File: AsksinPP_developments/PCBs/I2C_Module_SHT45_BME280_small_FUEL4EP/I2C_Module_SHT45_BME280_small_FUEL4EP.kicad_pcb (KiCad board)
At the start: 2 copper layers, 22 x 17 mm, 13 parts, among them J1 Conn_01x04, U1 BME280, U2 SHT45-AD1B-R2

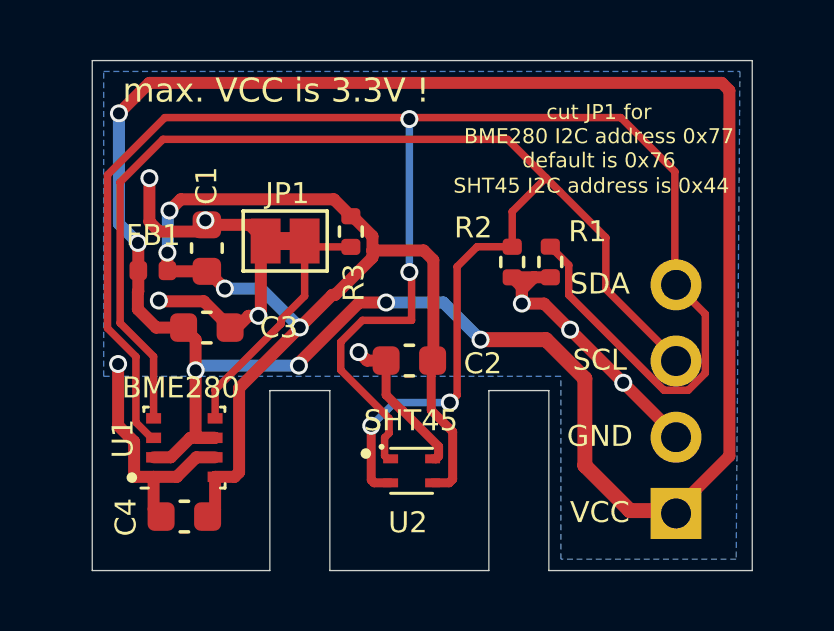
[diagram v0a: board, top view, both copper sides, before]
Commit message: PCBs: HB_Stamp_ATMega1284P_FUEL4EP and I2C_Module_SHT45_BME280_small_FUEL4EP: make I2C sockets fitting each other
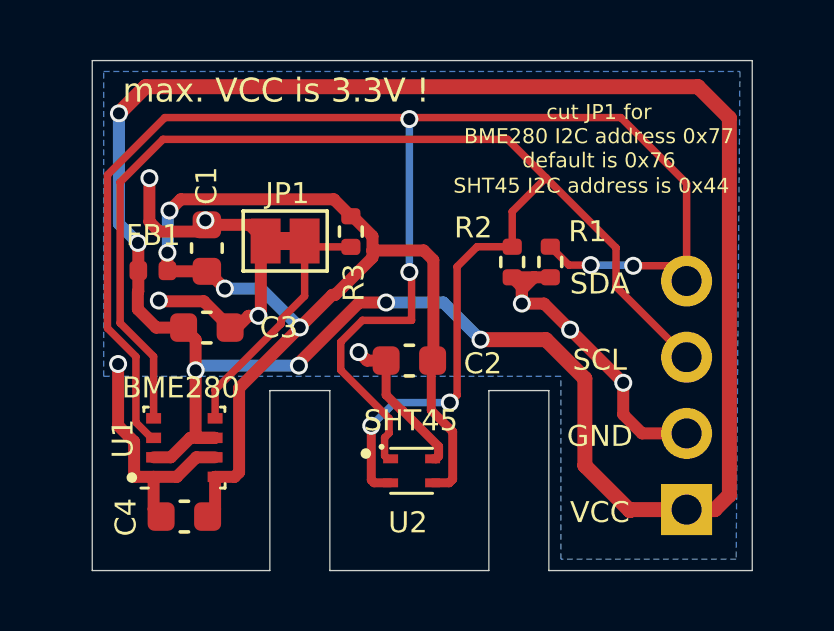
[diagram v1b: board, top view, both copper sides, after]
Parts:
- moved J1 0.37 mm to (19.8, -2.03)
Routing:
- net /SDA: track 59.0 -> 52.0 mm, vias 2 -> 4
- net GND: track 35.6 -> 36.3 mm
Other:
- board text added: "SHT45 BME280 I2C Modul small (C) FUEL4EP V1.1 01/2024"
- board text removed: "SHT45 BME280 I2C Modul small (C) FUEL4EP V1.0 01/2024"

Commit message: PCBs: fix of I2C Pull-up resistors that were wrongly tied to GND
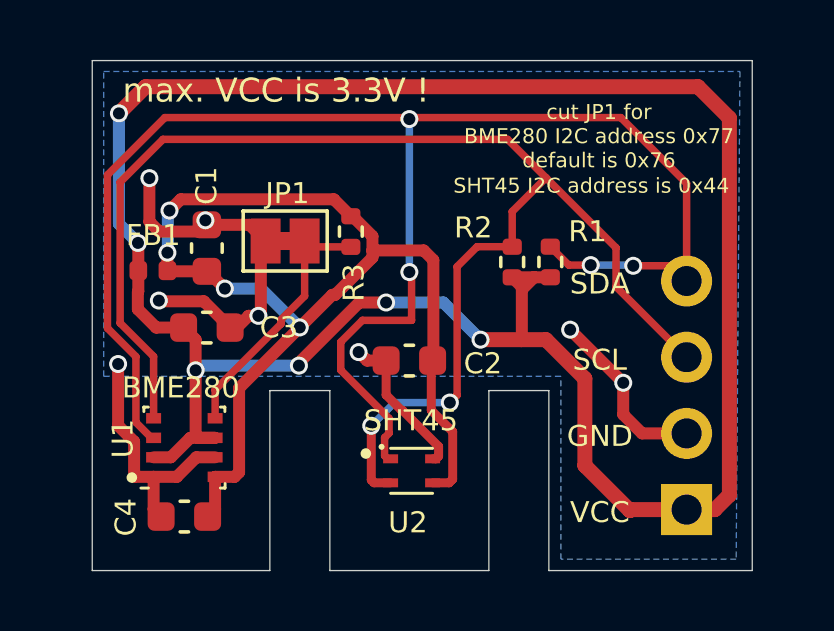
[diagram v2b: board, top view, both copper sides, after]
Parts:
- R1, R2: value 4.7k -> 10k
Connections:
- R1 pad 2: GND -> VCC
- R2 pad 2: GND -> VCC
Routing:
- net GND: track 36.3 -> 31.0 mm, vias 9 -> 8
- net VCC: track 72.6 -> 76.6 mm
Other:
- board text added: "SHT45 BME280 I2C Modul small (C) FUEL4EP V1.2 02/2024"
- board text removed: "SHT45 BME280 I2C Modul small (C) FUEL4EP V1.1 01/2024"
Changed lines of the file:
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@@
   (title_block
     (title "I2C_Module_SHT45_BME280_FUEL4EP")
-    (date "2023-12-15")
-    (rev "V1.1")
+    (date "2024-02-08")
+    (rev "V1.2")
     (company "(c) FUEL4EP")
   )
@@
     (descr "Resistor SMD 0402 (1005 Metric), square (rectangular) end terminal, IPC_7351 nominal, (Body size source: IPC-SM-782 page 72, https://www.pcb-3d.com/wordpress/wp-content/uploads/ipc-sm-782a_amendment_1_and_2.pdf), generated with kicad-footprint-generator")
     (tags "resistor")
-    (property "LCSC" "C25900")
+    (property "LCSC" "C25744")
     (property "Sheetfile" "I2C_Module_SHT45_BME280_small_FUEL4EP.kicad_sch")
     (property "Sheetname" "")
@@
       (effects (font (size 0.7 0.7) (thickness 0.15)))
     )
-    (fp_text value "4.7k" (at -0.12 -0.015 -270) (layer "F.Fab")
+    (fp_text value "10k" (at -0.12 -0.015 -270) (layer "F.Fab")
       (effects (font (size 0.7 0.7) (thickness 0.15)))
     )
@@
       (net 4 "/SDA") (pintype "passive"))
     (pad "2" smd roundrect (at 0.51 0 270) (size 0.54 0.64) (layers "F.Cu" "F.Paste" "F.Mask") (roundrect_rratio 0.25)
-      (net 2 "GND") (pintype "passive"))
+      (net 1 "VCC") (pintype "passive"))
     (model "${KICAD6_3DMODEL_DIR}/Resistor_SMD.3dshapes/R_0402_1005Metric.wrl"
       (offset (xyz 0 0 0))
@@
     (descr "Resistor SMD 0402 (1005 Metric), square (rectangular) end terminal, IPC_7351 nominal, (Body size source: IPC-SM-782 page 72, https://www.pcb-3d.com/wordpress/wp-content/uploads/ipc-sm-782a_amendment_1_and_2.pdf), generated with kicad-footprint-generator")
     (tags "resistor")
-    (property "LCSC" "C25900")
+    (property "LCSC" "C25744")
     (property "Sheetfile" "I2C_Module_SHT45_BME280_small_FUEL4EP.kicad_sch")
     (property "Sheetname" "")
@@
       (effects (font (size 0.7 0.7) (thickness 0.15)))
     )
-    (fp_text value "4.7k" (at -0.2 -0.1 -270) (layer "F.Fab")
+    (fp_text value "10k" (at -0.2 -0.1 -270) (layer "F.Fab")
       (effects (font (size 0.7 0.7) (thickness 0.15)))
     )
@@
       (net 3 "/SCL") (pintype "passive"))
     (pad "2" smd roundrect (at 0.51 0 270) (size 0.54 0.64) (layers "F.Cu" "F.Paste" "F.Mask") (roundrect_rratio 0.25)
-      (net 2 "GND") (pintype "passive"))
+      (net 1 "VCC") (pintype "passive"))
     (model "${KICAD6_3DMODEL_DIR}/Resistor_SMD.3dshapes/R_0402_1005Metric.wrl"
       (offset (xyz 0 0 0))
@@
   (gr_line (start 13.22 0) (end 7.92 0) (layer "Edge.Cuts") (width 0.0381))
   (gr_line (start 22 -17) (end 22 0) (layer "Edge.Cuts") (width 0.0381))
-  (gr_text "SHT45 BME280\nI2C Modul small\n(C) FUEL4EP\nV1.1\n01/2024" (at 10.795 -9.144) (layer "B.SilkS")
+  (gr_text "SHT45 BME280\nI2C Modul small\n(C) FUEL4EP\nV1.2\n02/2024" (at 10.795 -9.144) (layer "B.SilkS")
     (effects (font (size 0.7 0.7) (thickness 0.1524)) (justify mirror))
   )
@@
     (effects (font (size 0.8 0.8) (thickness 0.1524)))
   )
+  (segment (start 14.32 -7.716) (end 14.300884 -7.696884) (width 0.4) (layer "F.Cu") (net 1))
   (segment (start 17.92 -2) (end 16.42 -3.5) (width 0.5) (layer "F.Cu") (net 1))
   (segment (start 3.27 -4.425) (end 2.62 -3.775) (width 0.4) (layer "F.Cu") (net 1))
   (segment (start 8.900493 -8.935823) (end 9.794735 -8.935823) (width 0.4) (layer "F.Cu") (net 1))
   (segment (start 20.752 -2.032) (end 21.238 -2.518) (width 0.5) (layer "F.Cu") (net 1))
+  (segment (start 15.269 -9.777) (end 14.73 -9.777) (width 0.4) (layer "F.Cu") (net 1))
   (segment (start 21.238 -15.084) (end 20.193 -16.129) (width 0.5) (layer "F.Cu") (net 1))
   (segment (start 2.62 -3.775) (end 2.045 -3.775) (width 0.4) (layer "F.Cu") (net 1))
@@
   (segment (start 21.238 -2.518) (end 21.238 -15.084) (width 0.5) (layer "F.Cu") (net 1))
   (segment (start 17.92 -2) (end 17.952 -2.032) (width 0.5) (layer "F.Cu") (net 1))
+  (segment (start 14.32 -9.367) (end 14.73 -9.777) (width 0.4) (layer "F.Cu") (net 1))
+  (segment (start 14.73 -9.777) (end 14.001 -9.777) (width 0.4) (layer "F.Cu") (net 1))
   (segment (start 20.193 -16.129) (end 1.778 -16.129) (width 0.5) (layer "F.Cu") (net 1))
   (segment (start 17.952 -2.032) (end 19.812 -2.032) (width 0.5) (layer "F.Cu") (net 1))
-  (segment (start 15.123116 -7.696884) (end 12.9425 -7.696884) (width 0.5) (layer "F.Cu") (net 1))
   (segment (start 1.5205 -8.710257) (end 2.130757 -8.1) (width 0.4) (layer "F.Cu") (net 1))
   (segment (start 1.5205 -9.289743) (end 1.5205 -8.710257) (width 0.4) (layer "F.Cu") (net 1))
@@
   (segment (start 2.130757 -8.1) (end 3.045 -8.1) (width 0.4) (layer "F.Cu") (net 1))
   (segment (start 16.42 -6.4) (end 15.123116 -7.696884) (width 0.5) (layer "F.Cu") (net 1))
+  (segment (start 14.32 -9.454) (end 13.999 -9.775) (width 0.4) (layer "F.Cu") (net 1))
   (segment (start 1.535 -9.304243) (end 1.5205 -9.289743) (width 0.4) (layer "F.Cu") (net 1))
   (segment (start 3.52 -4.425) (end 3.445 -4.5) (width 0.4) (layer "F.Cu") (net 1))
   (segment (start 16.42 -3.5) (end 16.42 -6.4) (width 0.5) (layer "F.Cu") (net 1))
   (segment (start 1.535 -10) (end 1.535 -10.911) (width 0.4) (layer "F.Cu") (net 1))
+  (segment (start 14.32 -9.367) (end 14.32 -7.716) (width 0.4) (layer "F.Cu") (net 1))
   (segment (start 4.095 -4.425) (end 3.27 -4.425) (width 0.4) (layer "F.Cu") (net 1))
   (segment (start 3.445 -7.7) (end 3.045 -8.1) (width 0.4) (layer "F.Cu") (net 1))
   (segment (start 6.888742 -6.831258) (end 6.888742 -6.924072) (width 0.4) (layer "F.Cu") (net 1))
   (segment (start 4.095 -4.425) (end 3.52 -4.425) (width 0.4) (layer "F.Cu") (net 1))
+  (segment (start 14.300884 -7.696884) (end 12.9425 -7.696884) (width 0.5) (layer "F.Cu") (net 1))
   (segment (start 19.812 -2.032) (end 20.752 -2.032) (width 0.5) (layer "F.Cu") (net 1))
+  (segment (start 15.123116 -7.696884) (end 14.300884 -7.696884) (width 0.5) (layer "F.Cu") (net 1))
   (via (at 9.794735 -8.935823) (size 0.6) (drill 0.4) (layers "F.Cu" "B.Cu") (net 1))
   (via (at 1.524 -10.922) (size 0.6) (drill 0.4) (layers "F.Cu" "B.Cu") (net 1))
@@
   (segment (start 18.328 -4.572) (end 19.812 -4.572) (width 0.4) (layer "F.Cu") (net 2))
   (segment (start 11.457132 -3.725) (end 11.345 -3.725) (width 0.3) (layer "F.Cu") (net 2))
-  (segment (start 14.32 -8.9) (end 14.32 -9.454) (width 0.4) (layer "F.Cu") (net 2))
   (segment (start 5.62 -8.572728) (end 5.539014 -8.491742) (width 0.4) (layer "F.Cu") (net 2))
   (segment (start 10.316 -5.334) (end 9.795 -5.855) (width 0.3) (layer "F.Cu") (net 2))
@@
   (segment (start 10.348132 -5.334) (end 11.545 -4.137132) (width 0.3) (layer "F.Cu") (net 2))
   (segment (start 5.62 -10.825) (end 5.62 -8.572728) (width 0.4) (layer "F.Cu") (net 2))
-  (segment (start 15.269 -9.777) (end 14.73 -9.777) (width 0.4) (layer "F.Cu") (net 2))
   (segment (start 1.905 -11.625757) (end 1.905 -13.081) (width 0.4) (layer "F.Cu") (net 2))
   (segment (start 17.7 -6.26) (end 17.7 -5.2) (width 0.4) (layer "F.Cu") (net 2))
   (segment (start 5.211742 -8.491742) (end 5.539014 -8.491742) (width 0.4) (layer "F.Cu") (net 2))
-  (segment (start 15.93 -8.03) (end 15.06 -8.9) (width 0.4) (layer "F.Cu") (net 2))
-  (segment (start 14.32 -8.9) (end 14.32 -9.367) (width 0.4) (layer "F.Cu") (net 2))
-  (segment (start 14.32 -9.367) (end 14.73 -9.777) (width 0.4) (layer "F.Cu") (net 2))
-  (segment (start 14.73 -9.777) (end 14.001 -9.777) (width 0.4) (layer "F.Cu") (net 2))
   (segment (start 9.795 -5.855) (end 9.795 -7) (width 0.3) (layer "F.Cu") (net 2))
   (segment (start 2.230257 -11.3005) (end 1.905 -11.625757) (width 0.4) (layer "F.Cu") (net 2))
@@
   (segment (start 1.395 -3.125) (end 1.395 -4.299964) (width 0.4) (layer "F.Cu") (net 2))
   (segment (start 17.7 -6.26) (end 15.93 -8.03) (width 0.4) (layer "F.Cu") (net 2))
-  (segment (start 15.06 -8.9) (end 14.32 -8.9) (width 0.4) (layer "F.Cu") (net 2))
   (segment (start 4.595 -8.1) (end 3.72 -8.975) (width 0.4) (layer "F.Cu") (net 2))
   (segment (start 10.348132 -5.334) (end 10.316 -5.334) (width 0.3) (layer "F.Cu") (net 2))
-  (segment (start 14.32 -9.454) (end 13.999 -9.775) (width 0.4) (layer "F.Cu") (net 2))
   (segment (start 4.095 -3.775) (end 3.467822 -3.775) (width 0.4) (layer "F.Cu") (net 2))
   (segment (start 5.24 -11.525) (end 5.78 -10.985) (width 0.4) (layer "F.Cu") (net 2))
@@
   (via (at 1.905 -13.081) (size 0.6) (drill 0.4) (layers "F.Cu" "B.Cu") (net 2))
   (via (at 15.93 -8.03) (size 0.6) (drill 0.4) (layers "F.Cu" "B.Cu") (net 2))
-  (via (at 14.32 -8.9) (size 0.6) (drill 0.4) (layers "F.Cu" "B.Cu") (net 2))
   (via (at 2.22 -9) (size 0.6) (drill 0.4) (layers "F.Cu" "B.Cu") (net 2))
   (segment (start 11.92 -5.6) (end 12.162 -5.842) (width 0.25) (layer "F.Cu") (net 3))

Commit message: PCBs: I2C_Module_SHT45_BME280_small_FUEL4EP: shrinked x-size to 14.08 mm for geeting space for pogo-pin-adapter at mother board
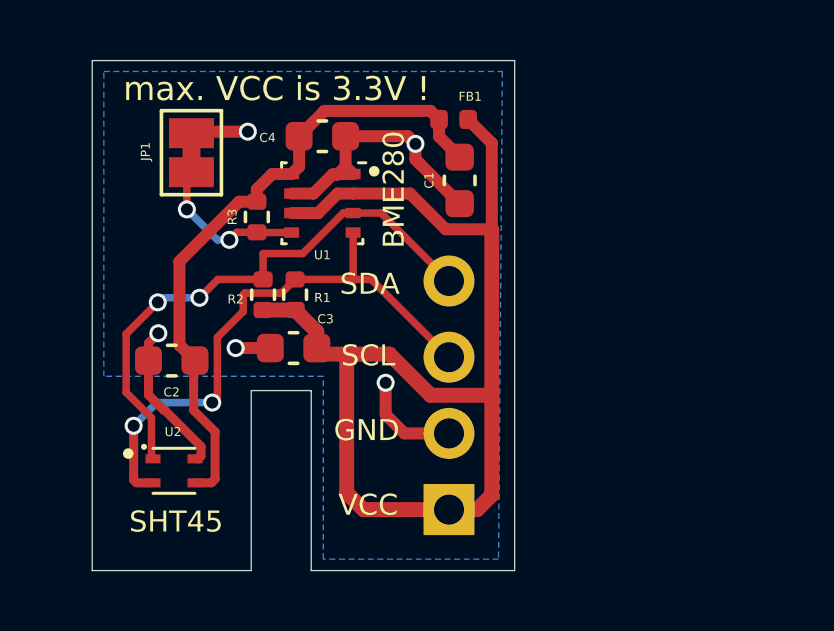
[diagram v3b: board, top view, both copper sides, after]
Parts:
- moved C4 13.5 mm to (7.67, -14.5), turned to 180 degrees
- moved FB1 11.2 mm to (12.0, -15.0), turned to 180 degrees
- moved LOGO1 10.4 mm to (2.85, -8.18), turned to -90 degrees
- moved R1 9.64 mm to (5.69, -9.19)
- moved U1 9.35 mm to (7.67, -12.2), turned to -90 degrees
- moved C1 8.72 mm to (12.2, -13.0), turned to -90 degrees
- moved J1 7.92 mm to (11.9, -2.03)
- moved C2 7.92 mm to (2.65, -7.00)
- moved U2 7.92 mm to (2.73, -3.33)
- moved R2 7.32 mm to (6.76, -9.19)
- moved JP1 4.29 mm to (3.31, -13.9), turned to -90 degrees
- moved R3 3.17 mm to (5.49, -11.8)
- moved C3 2.97 mm to (6.71, -7.42), turned to 0 degrees
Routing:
- net VCC: track 76.6 -> 39.3 mm, vias 6 -> 0
- net /SDA: track 52.0 -> 18.3 mm, vias 4 -> 2
- net /SCL: track 46.5 -> 19.2 mm
- net VDDA: track 37.0 -> 21.7 mm, vias 4 -> 0
- net GND: track 31.0 -> 20.7 mm, vias 8 -> 5
- net Net-(JP1-Pad2): track 8.49 -> 5.10 mm, vias 0 -> 2
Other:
- board size 22 x 17 mm -> 14.1 x 17 mm
- board text added: "SHT45 BME280 I2C Modul small (C) FUEL4EP V1.3 02/2024"
- board text removed: "SHT45 BME280 I2C Modul small (C) FUEL4EP V1.2 02/2024"
- board text removed: "SHT45 I2C address is 0x44"
- board text removed: "cut JP1 for BME280 I2C address 0x77 default is 0x76"

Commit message: PCBs: upgrade some PCBs to KiCAD 7; fix of unnecessary leakage current of I2C address selector: I2C_Module_SHT85_BME280_FUEL4EP, I2C_Module_SHT45_BME280_small_FUEL4EP, I2C_Module_SHT45_BME280_FUEL4EP, I2C_Module_BME280_FUEL4EP, and I2C_Module_BME680_FUEL4EP
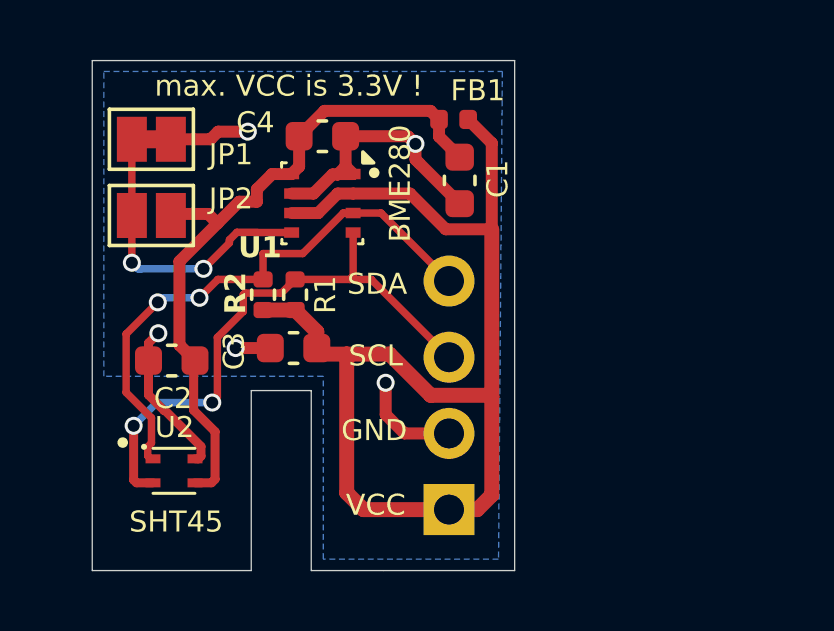
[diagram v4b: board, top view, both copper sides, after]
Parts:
- removed R3: 10k, Resistor_SMD:R_0402_1005Metric
- added JP2: SolderJumper_2_Open, Jumper:SolderJumper-2_P1.3mm_Open_Pad1.0x1.5mm, F.Cu at (1.97, -11.8)
- moved JP1 1.41 mm to (1.97, -14.4), turned to 180 degrees
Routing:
- net Net-(JP1-B): track 5.10 -> 10.1 mm
- net VDDA: track 21.7 -> 23.4 mm
- net GND: track 20.7 -> 21.6 mm
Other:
- board text added: "SHT45 BME280 I2C Modul small (C) FUEL4EP V1.4 04/2024"
- board text removed: "SHT45 BME280 I2C Modul small (C) FUEL4EP V1.3 02/2024"

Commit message: PCBs/I2C_Module_SHT45_BME280_small_FUEL4EP: migration to KiCAD 8
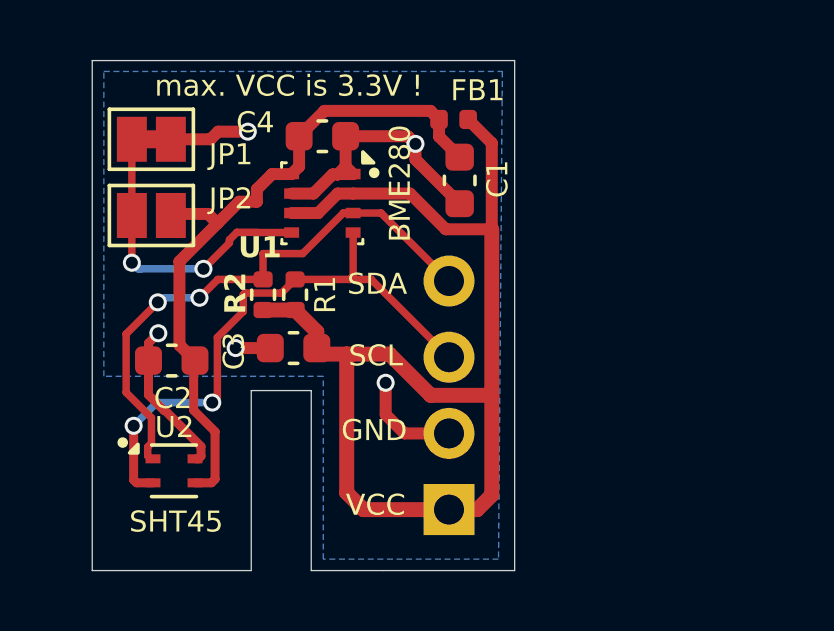
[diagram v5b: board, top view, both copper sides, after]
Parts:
- U2: footprint FUEL4EP:SHT4X -> Sensor_Humidity:Sensirion_DFN-4_1.5x1.5mm_P0.8mm_SHT4x_NoCentralPad
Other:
- board text added: "SHT45 BME280 I2C Modul small (C) FUEL4EP V1.5 09/2024"
- board text removed: "SHT45 BME280 I2C Modul small (C) FUEL4EP V1.4 04/2024"
